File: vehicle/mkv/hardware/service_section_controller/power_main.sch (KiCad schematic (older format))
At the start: 30 parts, among them U201 TPS560430YF

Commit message: incorporated feedback from dr
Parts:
- renumbered F204 to F203, F205 to F204, F206 to F205, F203 to F206, R205 to R204, R204 to R205
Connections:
- net +5V: now also TP208.1
- net at COUT201.1, COUT202.1, COUT203.1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: no longer TP208.1
- net 12V_BUCK renamed +12V_BUCK
- net 12V_IMD renamed +12V_IMD
- net 12V_SHUTDOWN renamed +12V_SHUTDOWN
- net 12V_TSAL renamed +12V_TSAL
- net 5V_AIR_CONTROL renamed +5V_AIR_CONTROL
- net 5V_BMS renamed +5V_BMS
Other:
- note added: "12-16V"
- note added: "POWER FLAGS"
- note removed: "(5V)"
- note removed: "12.8 - 16.8 V"
- moved on the sheet: F202, R205, TP201, TP202, TP208

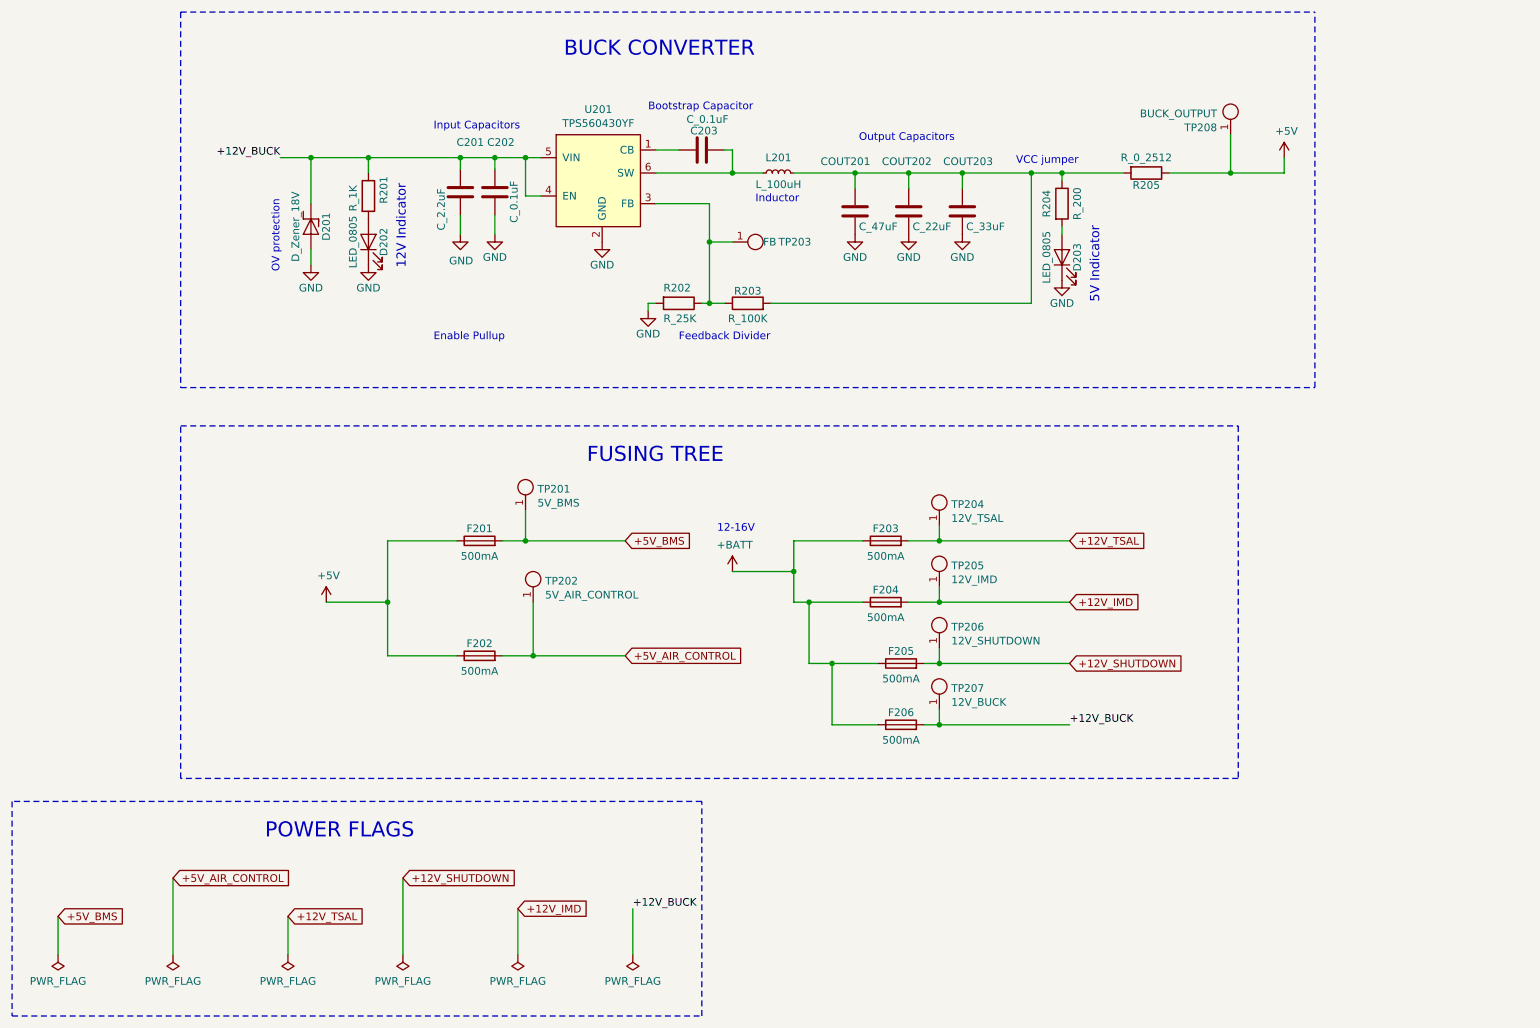
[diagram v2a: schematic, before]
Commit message: Update service section controller for rev 2 (#139)
* Made changes for Rev 2 of SS controller schematic and layout

changed 12V IMD net to 5V IMD
to make layout changes easier, 5V IMD is supplied after 5V AIR control fuse
Power Main: Added larger test points for +Batt and GND for easier testing
IMD Latch: changed 12V nets to 5V, swapped inverting and non-inverting inputs for both op amps, removed resistor divider at IMD_STATUS_OUTPUT that goes to the ATmega
TSAL/AIL: changed 12V_TSAL to a 5V input, changed ts+ side resistor dividers to 1k and 120 (bottom of the op amp), changed AIL logic to use an nmos
Power Secondary: removed HV lin reg, added 15V - 5V lin reg and added a fuse for the 5V output. 400-15V lin reg can be used to provide 15V OR we can change resistors to provide 5V and short the output of lin reg to the output of the buck.
Micros: added a programming header for isospi for easier firmware testing, added test points for CANH and CANL for firmware debugging.

* Updated rev number on back silkscreen of PCB

* Make changes to Rev 2 of Service Section Controller Schematic and Layout

Updated IMD Latch resistor dividers.
Changed 5V lin reg capacitors to 2 1uF capacitors.
Added a protection diode for lin reg.
Added a 0 Ohm jumper between 5V tsal and 15V buck output in case the buck converter can output 5V and we no longer need the lin reg.
Spread out the tsal resistors to help with heat dissipation.

* Added a few silkscreen labels for 0Ohm jumpers.

* Shifted connectors and edited track lengths

Changed IMD connector to a 6-pin microfit.
Rotated BMS connector to face upwards to avoid clearance issues.
added silkscreen for more clarity.

* Added final revisions for 2nd version of service section controller

Changed IMD connector to a RA footprint (same footprint as VT tho)
Changed Shutdown connector to an 8-pin RA microfit
Changed TS connector to a 4 pin VT microfit
shifted BMS connector slighly
changed bms and air control prog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
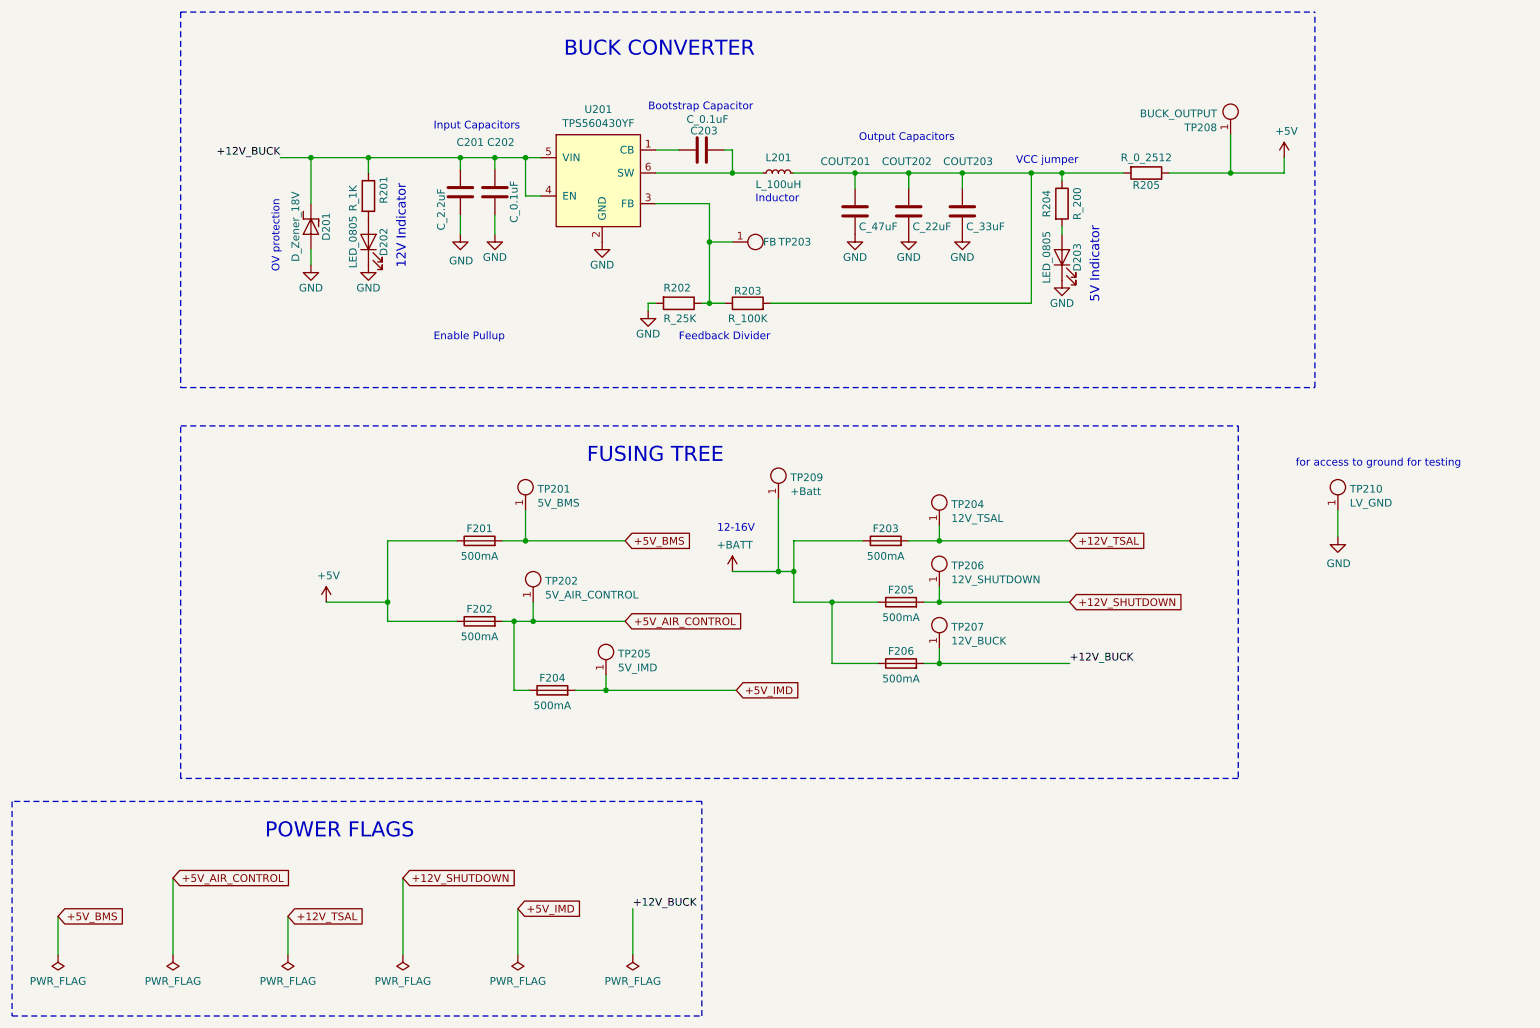
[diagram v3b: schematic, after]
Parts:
- added TP209: +Batt, TestPoint:TestPoint_Pad_D4.0mm, symbol formula:Test_Point_SMD
- added TP210: LV_GND, TestPoint:TestPoint_Pad_D4.0mm, symbol formula:Test_Point_SMD
- TP205: value 12V_IMD -> 5V_IMD
- TP208: footprint TestPoint:TestPoint_Pad_D1.0mm -> TestPoint:TestPoint_Pad_D4.0mm
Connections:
- net +5V_AIR_CONTROL: now also F204.1
- net +BATT: now also TP209.1; no longer F204.1
- net GND: now also TP210.1
- net +12V_IMD renamed +5V_IMD
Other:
- note added: "for access to ground for testing"
- moved on the sheet: F202, F204, F205, F206, TP205, TP206, TP207
